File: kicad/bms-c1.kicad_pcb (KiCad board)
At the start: 4 copper layers, 135 x 70 mm, 209 parts, among them J1 MicroFit 2x12, J2 B4B-PH-SM4, J3 USB_C_Receptacle_USB2.0, J4 B3B-PH-SM4, J5 B2B-PH-SM4, J6 B4B-PH-SM4, P1 CONN_01X01, P2 CONN_01X01, P3 CONN_01X01, P4 CONN_01X01, P5 CONN_01X01, Q1 DMN10H220LE, Q10 BSS84, Q11 BSS123N, Q12 ZXMP10A17GTA, Q2 IPT012N08N5, Q3 IPT012N08N5, Q4 IPT012N08N5, Q5 IPT012N08N5, Q6 IPT012N08N5, Q7 IPT012N08N5, Q8 IPT012N08N5, Q9 IPT012N08N5, U1 SN65HVD230, U2 SN65HVD75, U3 LMR38010, U4 BQ76952, U5 ESP32-C3-MINI-1

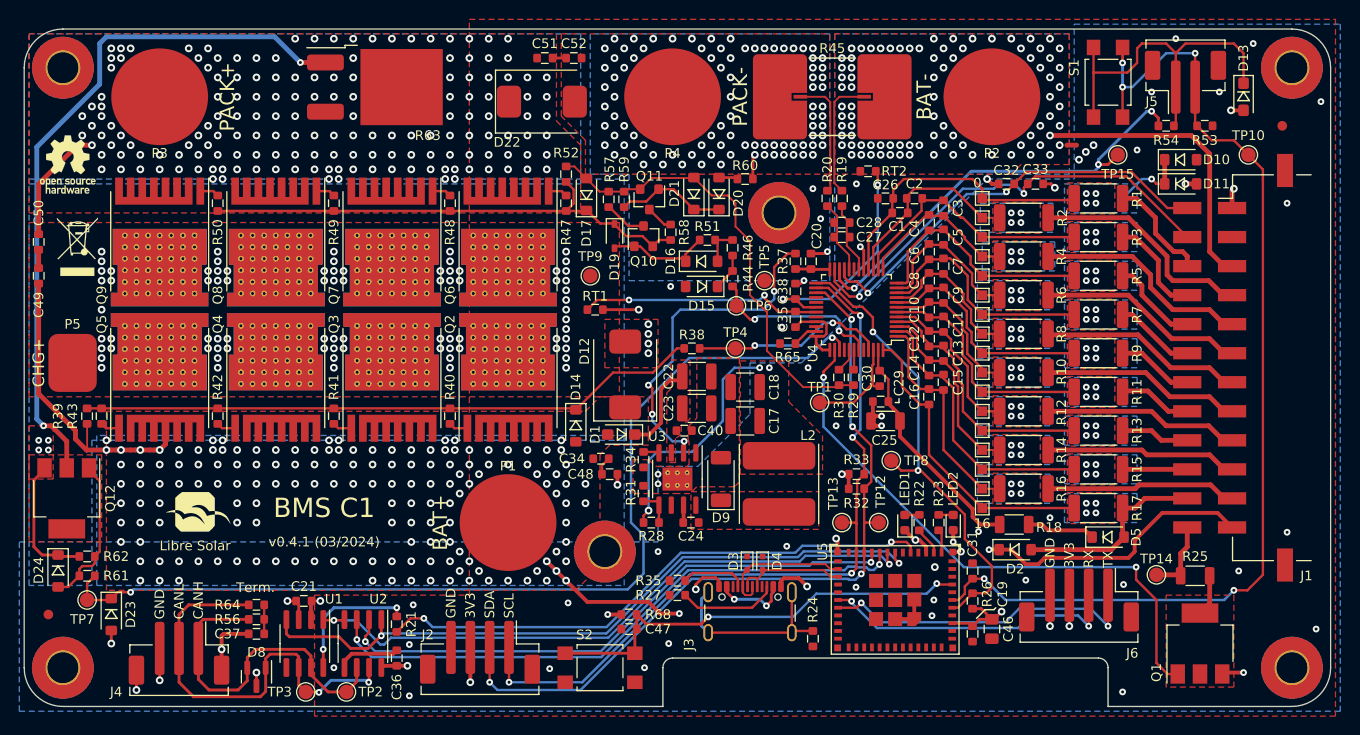
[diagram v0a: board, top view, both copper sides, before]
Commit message: power terminals THT, add mask
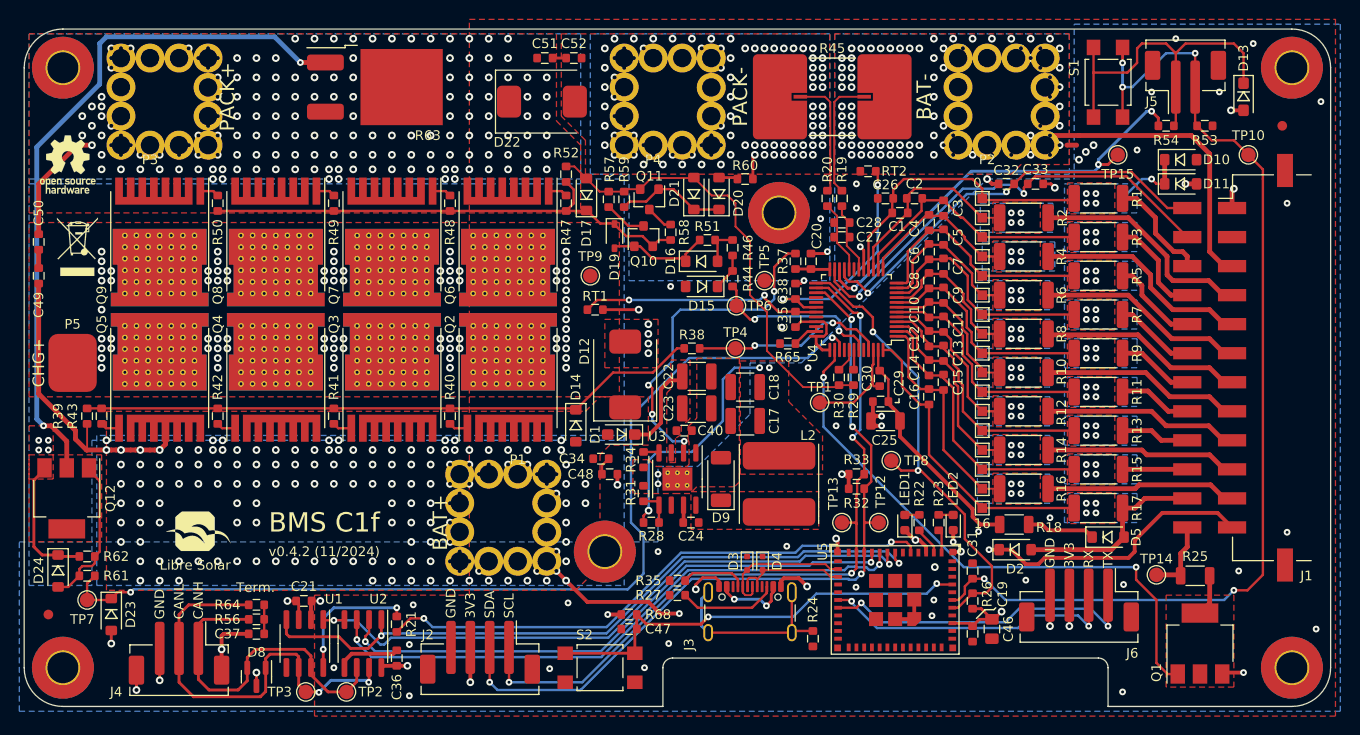
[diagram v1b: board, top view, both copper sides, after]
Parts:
- P1, P2, P3, P4: footprint LibreSolar:Wuerth_PowerOne_SMD_LF990005 -> open-pe:Wuerth_PowerPlus_M5_Nut
- moved P4 2.24 mm to (145.0, 56.0)
- moved LOGO2 2.00 mm to (95.7, 103.9)
- moved P1 1.41 mm to (131.0, 102.0)
- moved P3 1.41 mm to (93.0, 56.0)
- moved P2 1.12 mm to (179.5, 56.0)
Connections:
- J3 pad A4: unconnected-(J3-VBUS-PadA4) -> unconnected-(J3-VBUS-PadA4)_2
- J3 pad B4: unconnected-(J3-VBUS-PadA4) -> unconnected-(J3-VBUS-PadA4)_1
- J3 pad B9: unconnected-(J3-VBUS-PadA4) -> unconnected-(J3-VBUS-PadA4)_3
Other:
- board text added: "BMS C1f"
- board text added: "v0.4.2 (11/2024)"
- board text removed: "BMS C1"
- board text removed: "v0.4.1 (03/2024)"
